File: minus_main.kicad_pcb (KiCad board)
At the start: 2 copper layers, 158.8 x 86.4 mm, 8 parts, among them P1 CONN_01X05, P2 CONN_01X05, P3 CONN_01X02, P4 CONN_01X05, U1 socket_leon_x3_dil64, U2 socket_ams1117-3V3_mod, U4 socket_lm2596_mod

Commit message: minus: add a lots of pads for development
Signed-off-by: Yannick Gicquel <ygicquel@gmail.com>
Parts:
- added ? (x2): , Measurement_Points:Measurement_Point_Round-TH_Small, F.Cu at (152.4, 129.5)
- added ? (x2): , Measurement_Points:Measurement_Point_Round-TH_Small, F.Cu at (154.9, 132.1)
- added ? (x2): , Measurement_Points:Measurement_Point_Round-TH_Small, F.Cu at (157.5, 66.0)
- added ? (x2): , Measurement_Points:Measurement_Point_Round-TH_Small, F.Cu at (149.9, 66.0)
- added ? (x2): , Measurement_Points:Measurement_Point_Round-TH_Small, F.Cu at (154.9, 66.0)
- added ? (x2): , Measurement_Points:Measurement_Point_Round-TH_Small, F.Cu at (152.4, 66.0)
- added ? (x2): , Measurement_Points:Measurement_Point_Round-TH_Small, F.Cu at (152.4, 71.1)
- added ? (x2): , Measurement_Points:Measurement_Point_Round-TH_Small, F.Cu at (154.9, 71.1)
- added ? (x2): , Measurement_Points:Measurement_Point_Round-TH_Small, F.Cu at (149.9, 71.1)
- added ? (x2): , Measurement_Points:Measurement_Point_Round-TH_Small, F.Cu at (157.5, 71.1)
- added ? (x2): , Measurement_Points:Measurement_Point_Round-TH_Small, F.Cu at (149.9, 132.1)
- added ? (x2): , Measurement_Points:Measurement_Point_Round-TH_Small, F.Cu at (152.4, 68.6)
- added ? (x2): , Measurement_Points:Measurement_Point_Round-TH_Small, F.Cu at (154.9, 68.6)
- added ? (x2): , Measurement_Points:Measurement_Point_Round-TH_Small, F.Cu at (149.9, 68.6)
- added ? (x2): , Measurement_Points:Measurement_Point_Round-TH_Small, F.Cu at (157.5, 68.6)
- added ? (x2): , Measurement_Points:Measurement_Point_Round-TH_Small, F.Cu at (157.5, 132.1)
- added ? (x2): , Measurement_Points:Measurement_Point_Round-TH_Small, F.Cu at (152.4, 58.4)
- added ? (x2): , Measurement_Points:Measurement_Point_Round-TH_Small, F.Cu at (154.9, 58.4)
- added ? (x2): , Measurement_Points:Measurement_Point_Round-TH_Small, F.Cu at (149.9, 58.4)
- added ? (x2): , Measurement_Points:Measurement_Point_Round-TH_Small, F.Cu at (157.5, 58.4)
- added ? (x2): , Measurement_Points:Measurement_Point_Round-TH_Small, F.Cu at (152.4, 61.0)
- added ? (x2): , Measurement_Points:Measurement_Point_Round-TH_Small, F.Cu at (154.9, 61.0)
- added ? (x2): , Measurement_Points:Measurement_Point_Round-TH_Small, F.Cu at (149.9, 61.0)
- added ? (x2): , Measurement_Points:Measurement_Point_Round-TH_Small, F.Cu at (157.5, 61.0)
- added ? (x2): , Measurement_Points:Measurement_Point_Round-TH_Small, F.Cu at (152.4, 55.9)
- added ? (x2): , Measurement_Points:Measurement_Point_Round-TH_Small, F.Cu at (154.9, 55.9)
- added ? (x2): , Measurement_Points:Measurement_Point_Round-TH_Small, F.Cu at (149.9, 55.9)
- added ? (x2): , Measurement_Points:Measurement_Point_Round-TH_Small, F.Cu at (157.5, 55.9)
- added ? (x2): , Measurement_Points:Measurement_Point_Round-TH_Small, F.Cu at (152.4, 53.3)
- added ? (x2): , Measurement_Points:Measurement_Point_Round-TH_Small, F.Cu at (154.9, 53.3)
- added ? (x2): , Measurement_Points:Measurement_Point_Round-TH_Small, F.Cu at (149.9, 53.3)
- added ? (x2): , Measurement_Points:Measurement_Point_Round-TH_Small, F.Cu at (157.5, 53.3)
- added ? (x2): , Measurement_Points:Measurement_Point_Round-TH_Small, F.Cu at (152.4, 132.1)
- added ? (x2): , Measurement_Points:Measurement_Point_Round-TH_Small, F.Cu at (152.4, 127.0)
- added ? (x2): , Measurement_Points:Measurement_Point_Round-TH_Small, F.Cu at (154.9, 127.0)
- added ? (x2): , Measurement_Points:Measurement_Point_Round-TH_Small, F.Cu at (149.9, 127.0)
- added ? (x2): , Measurement_Points:Measurement_Point_Round-TH_Small, F.Cu at (154.9, 129.5)
- added ? (x2): , Measurement_Points:Measurement_Point_Round-TH_Small, F.Cu at (157.5, 127.0)
- added ? (x2): , Measurement_Points:Measurement_Point_Round-TH_Small, F.Cu at (152.4, 73.7)
- added ? (x2): , Measurement_Points:Measurement_Point_Round-TH_Small, F.Cu at (154.9, 73.7)
- added ? (x2): , Measurement_Points:Measurement_Point_Round-TH_Small, F.Cu at (149.9, 73.7)
- added ? (x2): , Measurement_Points:Measurement_Point_Round-TH_Small, F.Cu at (157.5, 73.7)
- added ? (x2): , Measurement_Points:Measurement_Point_Round-TH_Small, F.Cu at (149.9, 129.5)
- added ? (x2): , Measurement_Points:Measurement_Point_Round-TH_Small, F.Cu at (152.4, 76.2)
- added ? (x2): , Measurement_Points:Measurement_Point_Round-TH_Small, F.Cu at (154.9, 76.2)
- added ? (x2): , Measurement_Points:Measurement_Point_Round-TH_Small, F.Cu at (149.9, 76.2)
- added ? (x2): , Measurement_Points:Measurement_Point_Round-TH_Small, F.Cu at (157.5, 76.2)
- added ? (x2): , Measurement_Points:Measurement_Point_Round-TH_Small, F.Cu at (157.5, 129.5)
- added ? (x2): , Measurement_Points:Measurement_Point_Round-TH_Small, F.Cu at (152.4, 81.3)
- added ? (x2): , Measurement_Points:Measurement_Point_Round-TH_Small, F.Cu at (154.9, 81.3)
- added ? (x2): , Measurement_Points:Measurement_Point_Round-TH_Small, F.Cu at (149.9, 81.3)
- added ? (x2): , Measurement_Points:Measurement_Point_Round-TH_Small, F.Cu at (157.5, 81.3)
- added ? (x2): , Measurement_Points:Measurement_Point_Round-TH_Small, F.Cu at (152.4, 78.7)
- added ? (x2): , Measurement_Points:Measurement_Point_Round-TH_Small, F.Cu at (154.9, 78.7)
- added ? (x2): , Measurement_Points:Measurement_Point_Round-TH_Small, F.Cu at (149.9, 78.7)
- added ? (x2): , Measurement_Points:Measurement_Point_Round-TH_Small, F.Cu at (157.5, 78.7)
- added ? (x2): , Measurement_Points:Measurement_Point_Round-TH_Small, F.Cu at (152.4, 88.9)
- added ? (x2): , Measurement_Points:Measurement_Point_Round-TH_Small, F.Cu at (154.9, 88.9)
- added ? (x2): , Measurement_Points:Measurement_Point_Round-TH_Small, F.Cu at (149.9, 88.9)
- added ? (x2): , Measurement_Points:Measurement_Point_Round-TH_Small, F.Cu at (157.5, 88.9)
- added ? (x2): , Measurement_Points:Measurement_Point_Round-TH_Small, F.Cu at (152.4, 91.4)
- added ? (x2): , Measurement_Points:Measurement_Point_Round-TH_Small, F.Cu at (154.9, 91.4)
- added ? (x2): , Measurement_Points:Measurement_Point_Round-TH_Small, F.Cu at (149.9, 91.4)
- added ? (x2): , Measurement_Points:Measurement_Point_Round-TH_Small, F.Cu at (157.5, 91.4)
- added ? (x2): , Measurement_Points:Measurement_Point_Round-TH_Small, F.Cu at (152.4, 86.4)
- added ? (x2): , Measurement_Points:Measurement_Point_Round-TH_Small, F.Cu at (154.9, 86.4)
- added ? (x2): , Measurement_Points:Measurement_Point_Round-TH_Small, F.Cu at (149.9, 86.4)
- added ? (x2): , Measurement_Points:Measurement_Point_Round-TH_Small, F.Cu at (157.5, 86.4)
- added ? (x2): , Measurement_Points:Measurement_Point_Round-TH_Small, F.Cu at (152.4, 83.8)
- added ? (x2): , Measurement_Points:Measurement_Point_Round-TH_Small, F.Cu at (154.9, 83.8)
- added ? (x2): , Measurement_Points:Measurement_Point_Round-TH_Small, F.Cu at (149.9, 83.8)
- added ? (x2): , Measurement_Points:Measurement_Point_Round-TH_Small, F.Cu at (157.5, 83.8)
- added ? (x2): , Measurement_Points:Measurement_Point_Round-TH_Small, F.Cu at (152.4, 63.5)
- added ? (x2): , Measurement_Points:Measurement_Point_Round-TH_Small, F.Cu at (154.9, 63.5)
- added ? (x2): , Measurement_Points:Measurement_Point_Round-TH_Small, F.Cu at (149.9, 63.5)
- added ? (x2): , Measurement_Points:Measurement_Point_Round-TH_Small, F.Cu at (157.5, 63.5)
- added REF**: Measurement_Point_Round-TH_Small, Measurement_Points:Measurement_Point_Round-TH_Small, F.Cu at (139.7, 121.9)
- added REF**: Measurement_Point_Round-TH_Small, Measurement_Points:Measurement_Point_Round-TH_Small, F.Cu at (139.7, 124.5)
- added REF**: Measurement_Point_Round-TH_Small, Measurement_Points:Measurement_Point_Round-TH_Small, F.Cu at (94.0, 121.9)
- added REF**: Measurement_Point_Round-TH_Small, Measurement_Points:Measurement_Point_Round-TH_Small, F.Cu at (91.4, 124.5)

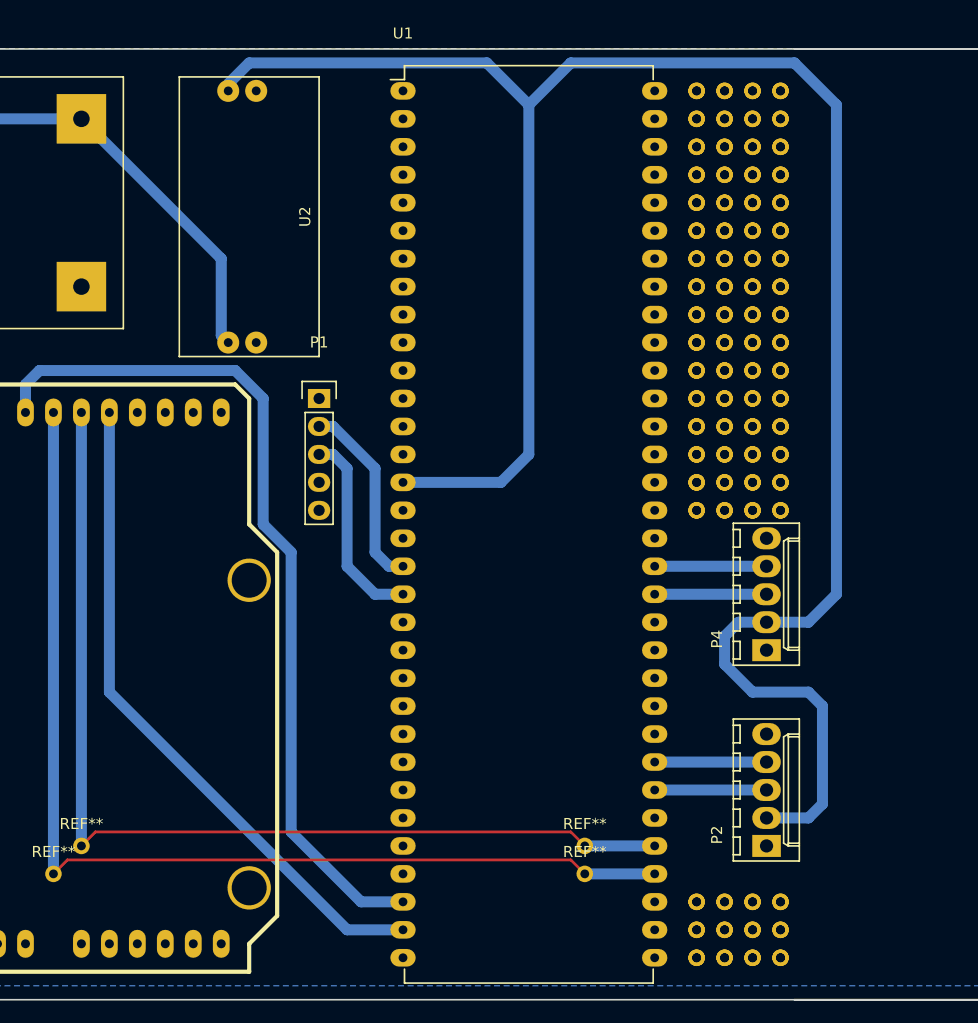
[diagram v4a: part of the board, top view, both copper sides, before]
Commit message: minus: add BT HC-05 module on schematic & pcb
Signed-off-by: Yannick Gicquel <ygicquel@gmail.com>
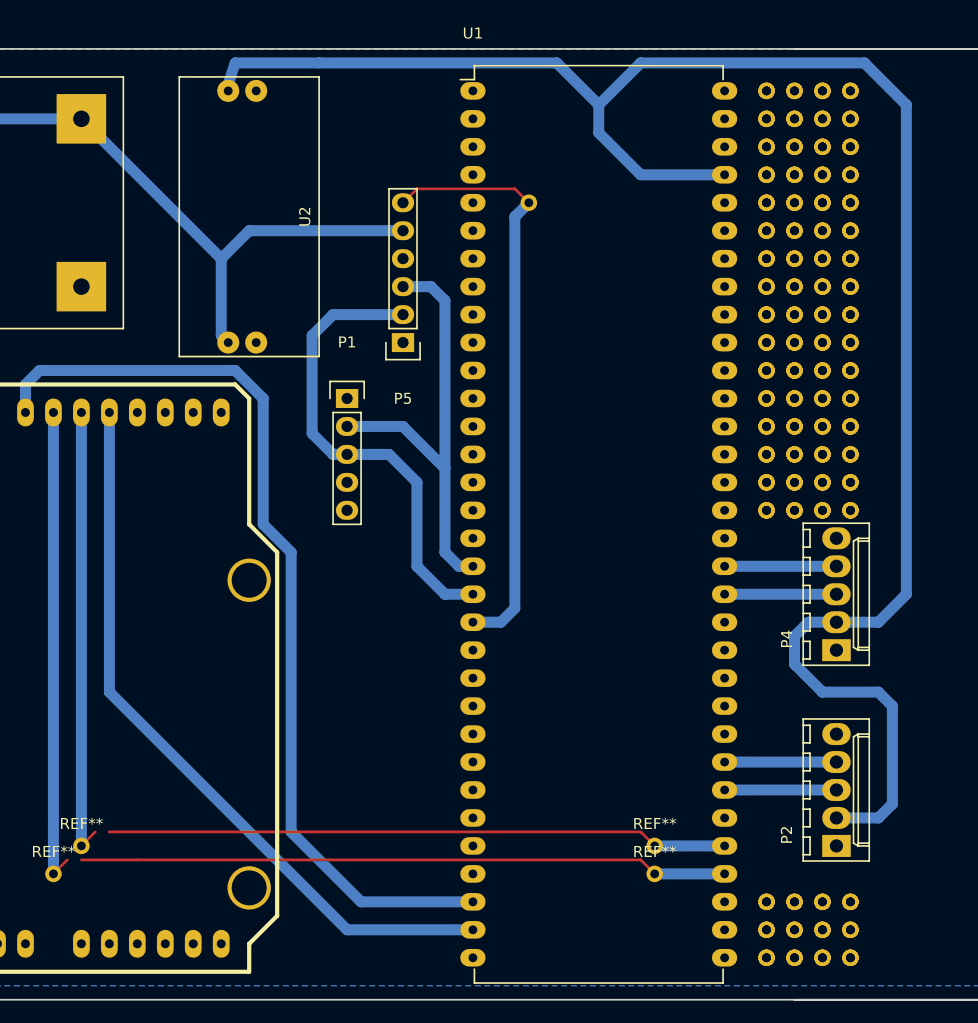
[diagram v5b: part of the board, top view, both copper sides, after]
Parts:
- added ?: , Measurement_Points:Measurement_Point_Round-TH_Small, F.Cu at (134.6, 63.5)
- added P5: CONN_01X06, Pin_Headers:Pin_Header_Straight_1x06, F.Cu at (123.2, 76.2)
- moved ? 6.35 mm to (163.8, 66.0) (x2)
- moved ? 6.35 mm to (163.8, 71.1) (x2)
- moved ? 6.35 mm to (163.8, 68.6) (x2)
- moved ? 6.35 mm to (163.8, 58.4) (x2)
- moved ? 6.35 mm to (163.8, 132.1) (x2)
- moved ? 6.35 mm to (163.8, 61.0) (x2)
- moved ? 6.35 mm to (163.8, 55.9) (x2)
- moved ? 6.35 mm to (163.8, 53.3)
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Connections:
- net /Sheet_Connectors/UART_DBG_RXD renamed /Sheet_Connectors/BT_RXD
- net /Sheet_Connectors/UART_DBG_TXD renamed /Sheet_Connectors/BT_TXD
- U1 pad 15: +3V3 -> Net-(U1-Pad15)
- U1 pad 20: Net-(U1-Pad20) -> /Sheet_Connectors/BT_KEY
- U1 pad 24: Net-(U1-Pad24) -> GND
- U1 pad 34: Net-(U1-Pad34) -> GND
- U1 pad 44: Net-(U1-Pad44) -> GND
- U1 pad 52: Net-(U1-Pad52) -> GND
- U1 pad 60: Net-(U1-Pad60) -> GND
- U1 pad 61: Net-(U1-Pad61) -> +3V3
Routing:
- net (no net): track 0.00 -> 115.4 mm, vias 0 -> 2
- net /Sheet_Connectors/BT_KEY: track 0.00 -> 54.2 mm, vias 0 -> 1
- net /Sheet_MCU/PWM_L: track 97.6 -> 43.7 mm, vias 2 -> 1
- net /Sheet_MCU/PWM_R: track 92.5 -> 41.2 mm, vias 2 -> 1
- net /Sheet_Connectors/BT_RXD: track 18.1 -> 43.1 mm
- net /Sheet_Connectors/BT_TXD: track 17.3 -> 40.7 mm
- net +3V3: track 189.3 -> 167.6 mm
- net +5V: track 137.9 -> 155.4 mm
- net /Sheet_MCU/DIR_L: track 78.9 -> 85.3 mm
- net /Sheet_MCU/DIR_R: track 61.0 -> 67.4 mm

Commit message: minus: add a GND testpad
This is intented to get an easy access to GND reference
for electrical measurement on board.

Signed-off-by: Yannick Gicquel <ygicquel@gmail.com>
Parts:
- added W1: TEST_1P, Pin_Headers:Pin_Header_Straight_1x01, F.Cu at (120.7, 110.5)
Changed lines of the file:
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@@
 (kicad_pcb (version 4) (host pcbnew 4.0.4+e1-6308~48~ubuntu16.04.1-stable)
   (general
-    (links 36)
+    (links 37)
     (no_connects 4)
     (area 35.484999 49.454999 194.385001 135.965001)
@@
     (tracks 96)
     (zones 0)
-    (modules 166)
+    (modules 167)
     (nets 88)
   )
@@
   )
   (setup
-    (last_trace_width 1)
+    (last_trace_width 0.25)
     (user_trace_width 0.5)
     (user_trace_width 0.75)
@@
     )
   )
+  (module Pin_Headers:Pin_Header_Straight_1x01 (layer F.Cu)
+    (at 120.65 110.49)
+    (descr "Through hole pin header")
+    (tags "pin header")
+    (fp_text reference W1 (at 0 -5.1) (layer F.SilkS)
+      (effects (font (size 1 1) (thickness 0.15)))
+    )
+    (fp_text value TEST_1P (at 0 -3.1) (layer F.Fab)
+      (effects (font (size 1 1) (thickness 0.15)))
+    )
+    (fp_line (start 1.55 -1.55) (end 1.55 0) (layer F.SilkS) (width 0.15))
+    (fp_line (start -1.75 -1.75) (end -1.75 1.75) (layer F.CrtYd) (width 0.05))
+    (fp_line (start 1.75 -1.75) (end 1.75 1.75) (layer F.CrtYd) (width 0.05))
+    (fp_line (start -1.75 -1.75) (end 1.75 -1.75) (layer F.CrtYd) (width 0.05))
+    (fp_line (start -1.75 1.75) (end 1.75 1.75) (layer F.CrtYd) (width 0.05))
+    (fp_line (start -1.55 0) (end -1.55 -1.55) (layer F.SilkS) (width 0.15))
+    (fp_line (start -1.55 -1.55) (end 1.55 -1.55) (layer F.SilkS) (width 0.15))
+    (fp_line (start -1.27 1.27) (end 1.27 1.27) (layer F.SilkS) (width 0.15))
+    (pad 1 thru_hole rect (at 0 0) (size 2.2352 2.2352) (drill 1.016) (layers *.Cu *.Mask F.SilkS)
+      (net 47 GND))
+    (model Pin_Headers.3dshapes/Pin_Header_Straight_1x01.wrl
+      (at (xyz 0 0 0))
+      (scale (xyz 1 1 1))
+      (rotate (xyz 0 0 90))
+    )
+  )
   (gr_text "Minus Bot\n2016\nV1" (at 41.91 72.39 90) (layer B.Cu)
     (effects (font (size 2 2) (thickness 0.375)) (justify left mirror))
@@
   (segment (start 140.97 57.15) (end 140.97 54.61) (width 1) (layer B.Cu) (net 48))
   (segment (start 144.78 60.96) (end 140.97 57.15) (width 1) (layer B.Cu) (net 48))
-  (segment (start 152.4 60.96) (end 144.78 60.96) (width 1) (layer B.Cu) (net 48) (status 400000))
+  (segment (start 152.4 60.96) (end 144.78 60.96) (width 1) (layer B.Cu) (net 48))
   (segment (start 115.57 50.8) (end 107.95 50.8) (width 1) (layer B.Cu) (net 48))
   (segment (start 140.97 54.61) (end 137.16 50.8) (width 1) (layer B.Cu) (net 48))
@@
   (segment (start 116.84 73.66) (end 114.935 75.565) (width 1) (layer B.Cu) (net 84))
   (segment (start 116.84 86.36) (end 121.92 86.36) (width 1) (layer B.Cu) (net 84))
-  (segment (start 127 99.06) (end 129.54 99.06) (width 1) (layer B.Cu) (net 84) (status 800000))
+  (segment (start 127 99.06) (end 129.54 99.06) (width 1) (layer B.Cu) (net 84))
   (segment (start 124.46 96.52) (end 127 99.06) (width 1) (layer B.Cu) (net 84))
   (segment (start 124.46 88.9) (end 124.46 96.52) (width 1) (layer B.Cu) (net 84))
